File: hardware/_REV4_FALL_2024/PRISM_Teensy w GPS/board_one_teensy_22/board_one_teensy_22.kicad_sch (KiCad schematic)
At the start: 31 parts, among them J1 Micro_SD_Card_Det_Hirose_DM3AT, J3 3387, Q1 AO3400A, Q2 AO3400A, U1 Teensy4.0, U2 GPS-14414, U3 3966, U4 RFM69HCW_Breakout, U5 CT25E-16T150-1, U6 CMI-9605-1280T

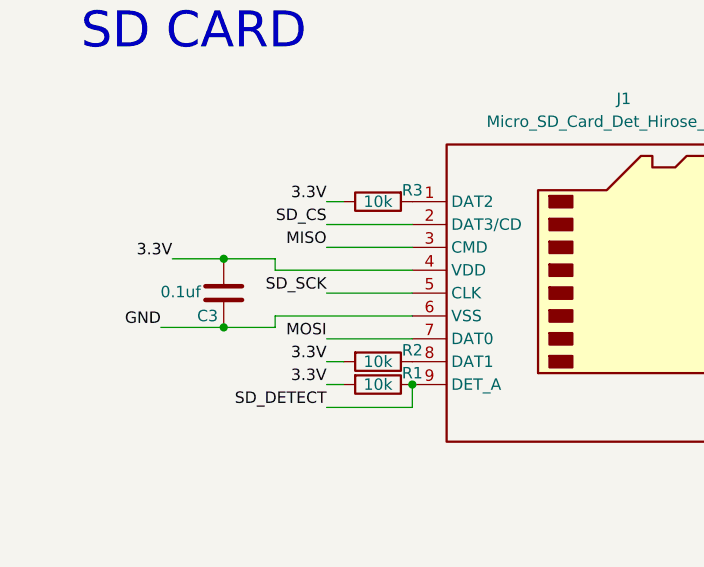
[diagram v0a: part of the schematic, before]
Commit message: Fixed PRISM SD Card
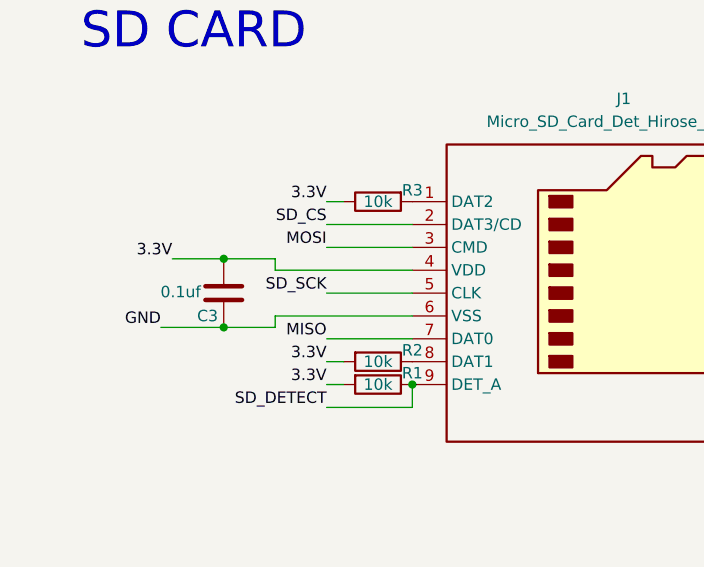
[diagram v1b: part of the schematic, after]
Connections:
- net MISO: now also J1.7 (DAT0); no longer J1.3 (CMD)
- net MOSI: now also J1.3 (CMD); no longer J1.7 (DAT0)
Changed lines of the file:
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@@
     (effects (font (size 1.27 1.27)) (justify left bottom))
-  )
-  (label "MISO" (at 46.355 162.56 180) (fields_autoplaced)
-    (effects (font (size 1.27 1.27)) (justify right bottom))
   )
   (label "SCL" (at 133.35 100.33 180) (fields_autoplaced)
@@
     (effects (font (size 1.27 1.27)) (justify left bottom))
   )
-  (label "MOSI" (at 46.355 172.72 180) (fields_autoplaced)
-    (effects (font (size 1.27 1.27)) (justify right bottom))
-  )
   (label "GND" (at 80.01 59.69 0) (fields_autoplaced)
     (effects (font (size 1.27 1.27)) (justify left bottom))
@@
   (label "SDA" (at 80.01 77.47 0) (fields_autoplaced)
     (effects (font (size 1.27 1.27)) (justify left bottom))
+  )
+  (label "MOSI" (at 46.355 162.56 180) (fields_autoplaced)
+    (effects (font (size 1.27 1.27)) (justify right bottom))
   )
   (label "NEOPIXEL" (at 241.3 33.02 180) (fields_autoplaced)
@@
     (effects (font (size 1.27 1.27)) (justify right bottom))
   )
+  (label "MISO" (at 46.355 172.72 180) (fields_autoplaced)
+    (effects (font (size 1.27 1.27)) (justify right bottom))
+  )
